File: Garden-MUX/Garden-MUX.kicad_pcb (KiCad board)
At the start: 2 copper layers, 46 x 46 mm, 54 parts, among them J1 USB_C_Receptacle_USB2.0_16P, J2 SDCARD_MODULE, P1 S2B-PH-SM4-TB, Q1 AO3401A, U2 MCP73832-2-OT, U3 AP2112K-3.3, U4 AP2112K-3.3, U5 ESP32-C6-MINI-1

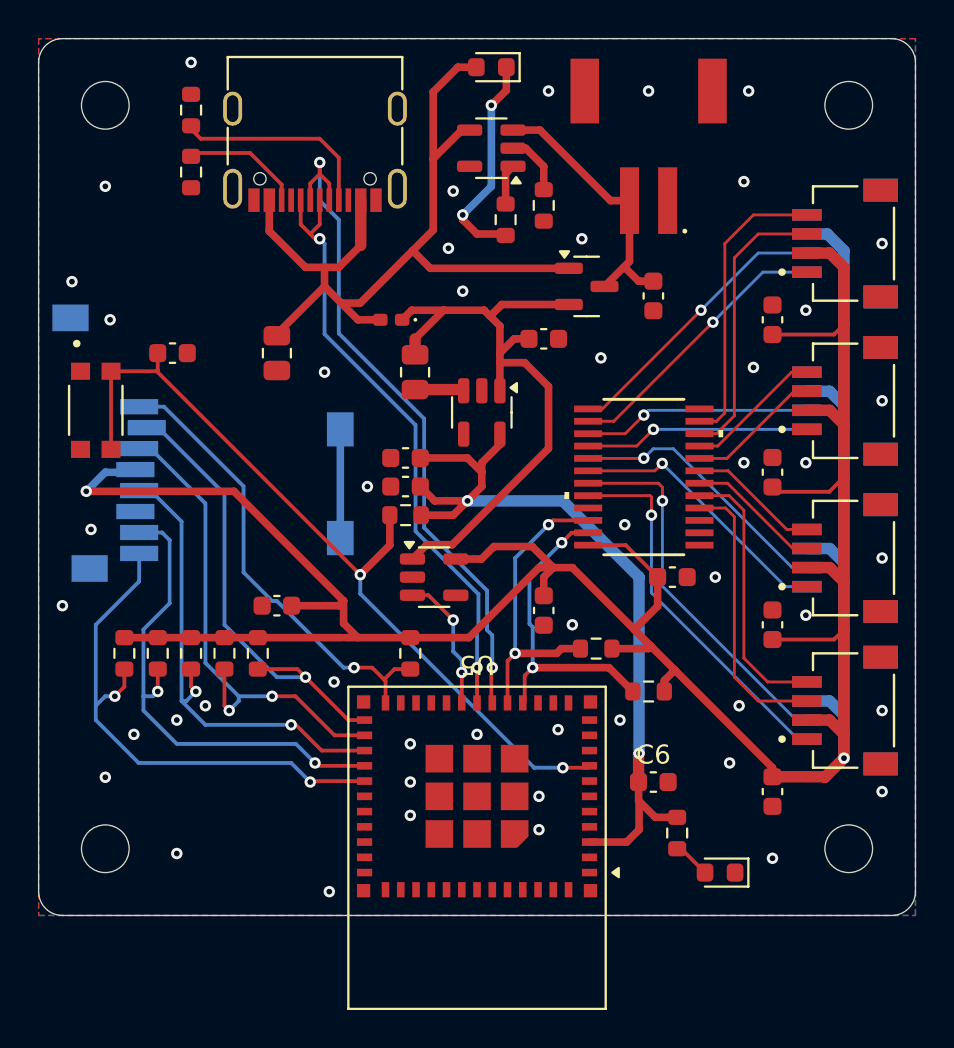
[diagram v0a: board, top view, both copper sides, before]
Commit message: Add boot button and adjust 3D models
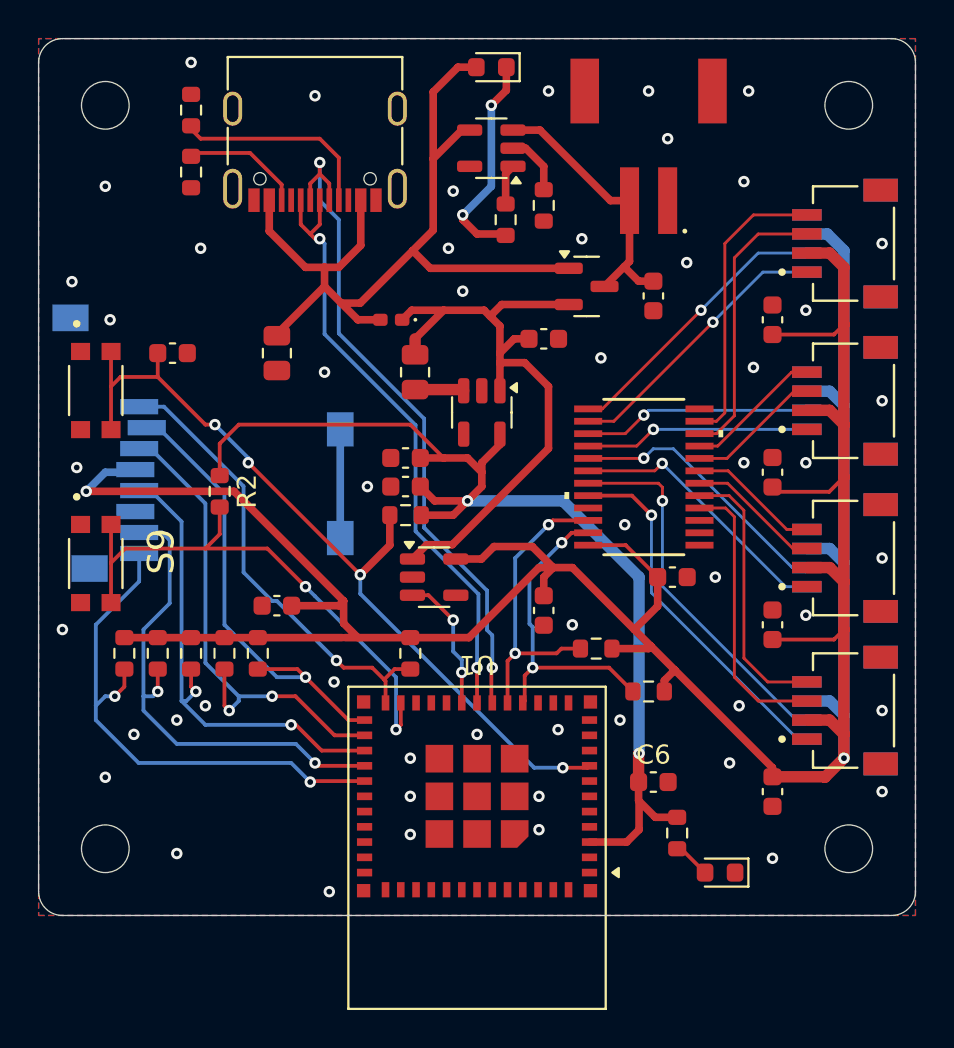
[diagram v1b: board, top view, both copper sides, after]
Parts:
- added R2: 100k, Resistor_SMD:R_0603_1608Metric, F.Cu at (140.8, 86.0)
- added S9: TL6330AF200Q, Pico_Footprints:SW_TL6330AF200Q_Footprint, F.Cu at (134.2, 89.8)
- moved S10 1.04 mm to (134.2, 80.7)
- renumbered C23 to C10, C24 to C11, C25 to C12, C26 to C13, C19 to C7, C20 to C8, C21 to C9, R20 to R1, R12 to R10, R13 to R11, R14 to R12, R15 to R13, R16 to R14, R17 to R15, R18 to R16, R19 to R17, R2 to R3, R3 to R4, R4 to R5, R8 to R7, R10 to R8, R11 to R9, S11 to S10, U5 to U1
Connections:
- U1 pad 23: unconnected-(U5-IO9-Pad23) -> /BOOT
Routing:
- net /BOOT: track 0.00 -> 28.9 mm, vias 0 -> 2
- net +3.3V: track 42.4 -> 57.0 mm
- net /SCL7: track 19.7 -> 19.1 mm
- net /RST: track 43.2 -> 43.7 mm, vias 2 -> 4
- net GND: vias 48 -> 52

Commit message: Add name silkscreen
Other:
- board text added: "DESGINED BY ARMANDO MARTINEZ"
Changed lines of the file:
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@@
 		(layer "Edge.Cuts")
+	)
+	(gr_text "DESGINED BY ARMANDO MARTINEZ"
+		(at 166.2 106.735 0)
+		(layer "B.SilkS" knockout)
+		(effects
+			(font
+				(size 1 1)
+				(thickness 0.25)
+				(bold yes)
+			)
+			(justify left bottom mirror)
+		)
 	)
 	(dimension
